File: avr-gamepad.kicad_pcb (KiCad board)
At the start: 2 copper layers, 29.7 x 55.6 mm, 31 parts, among them J1 Conn_01x08, P1 USB_C_Plug_USB2.0, SW10 Up, SW11 Down, SW12 Left, SW13 Select, SW2 R, SW3 X, SW4 A, SW5 B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

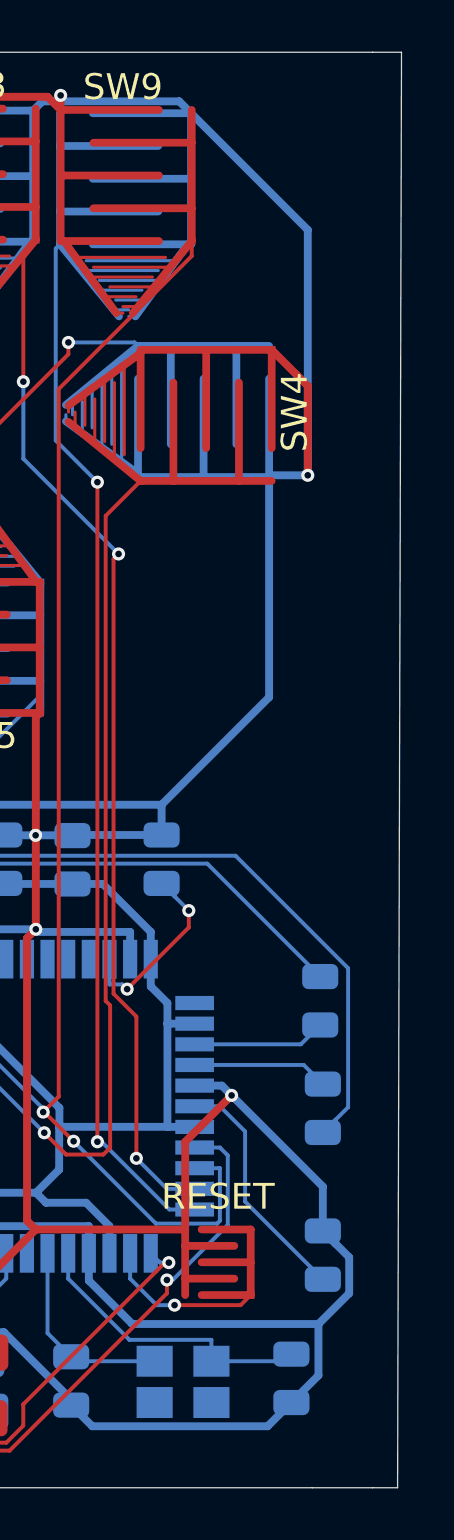
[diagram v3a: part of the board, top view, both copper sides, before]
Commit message: reduce outline
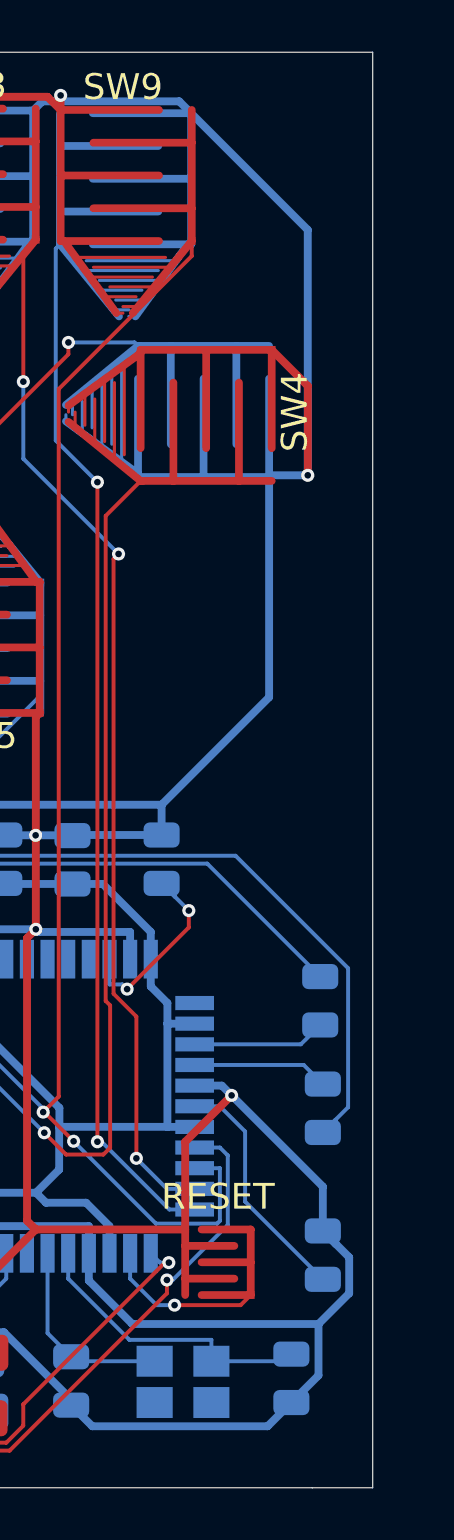
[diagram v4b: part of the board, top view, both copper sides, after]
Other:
- board size 29.7 x 55.6 mm -> 28.5 x 55.6 mm
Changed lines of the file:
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@@
   (general
     (thickness 0.1016)
-    (drawings 21)
+    (drawings 19)
     (tracks 490)
     (zones 0)
@@
       ))
   )
-  (gr_line (start 156.972 136.0424) (end 156.0068 136.0424) (layer Edge.Cuts) (width 0.05))
-  (gr_line (start 157.1244 80.4164) (end 156.972 136.0424) (layer Edge.Cuts) (width 0.05))
-  (gr_line (start 156.0068 80.4164) (end 157.1244 80.4164) (layer Edge.Cuts) (width 0.05))
+  (gr_line (start 156.0068 136.0424) (end 156.0068 80.4164) (layer Edge.Cuts) (width 0.05))
   (gr_line (start 127.4572 80.4164) (end 127.4826 102.0826) (layer Edge.Cuts) (width 0.05))
   (gr_line (start 127.4572 80.4164) (end 156.0068 80.4164) (layer Edge.Cuts) (width 0.05))

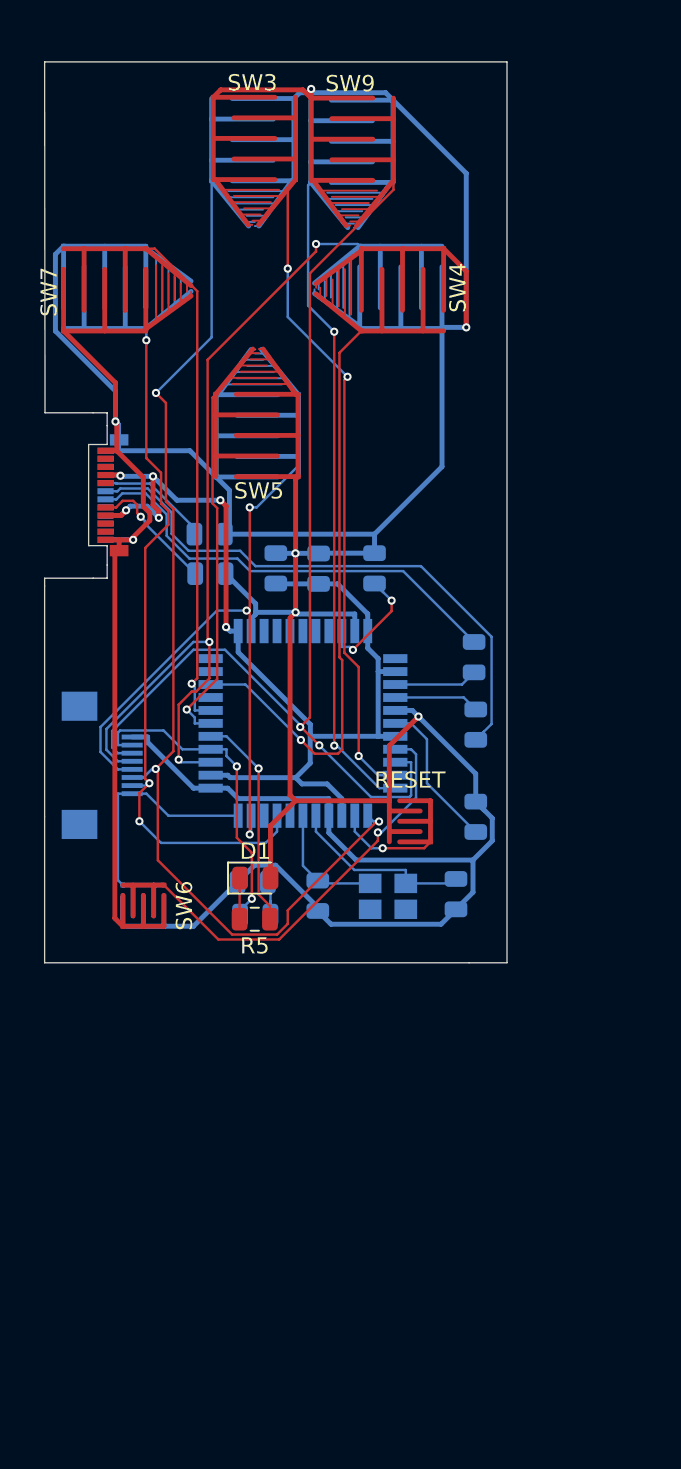
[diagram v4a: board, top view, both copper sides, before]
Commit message: pin swapping and component shuffling
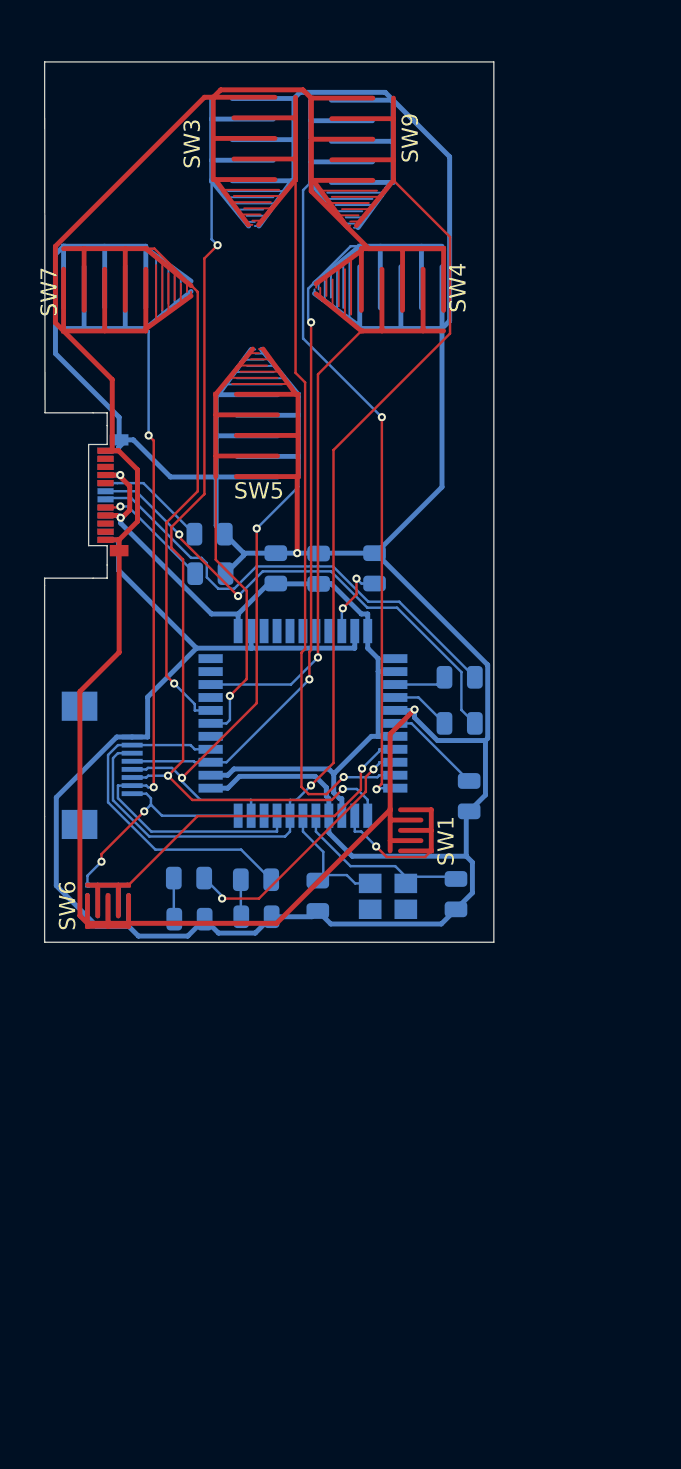
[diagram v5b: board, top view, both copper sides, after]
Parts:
- D1, R5: moved to B.Cu
- moved D1 4.79 mm to (136.4, 133.3)
- moved R5 4.79 mm to (136.4, 130.8)
- moved R6 2.18 mm to (140.5, 130.9), turned to 0 degrees
- moved SW13 2.18 mm to (131.4, 132.5)
- moved SW6 2.18 mm to (131.4, 132.5)
- moved D2 2.15 mm to (140.5, 133.2), turned to 0 degrees
- moved R4 1.53 mm to (153.1, 118.4), turned to 0 degrees
- moved C8 1.34 mm to (153.7, 125.8), turned to 270 degrees
- moved R2 1.00 mm to (153.1, 121.3), turned to 0 degrees
- moved SW1 0.56 mm to (150.1, 127.9)
- renumbered RESET to SW1
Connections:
- J1 pad 6: /pb1 -> /pd0
- R5 pad 2: /pd7 -> /pb1
- SW9 pad 1: /pb1 -> /pd0
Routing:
- net /pd0: track 0.00 -> 61.9 mm, vias 0 -> 1
- net GND: track 250.8 -> 312.4 mm, vias 7 -> 2
- net /pb1: track 66.0 -> 16.5 mm
- net +5V: track 67.1 -> 51.9 mm, vias 6 -> 2
- net /pd7: track 13.8 -> 0.00 mm, vias 1 -> 0
- net /pd4: track 52.1 -> 41.6 mm, vias 3 -> 2
- net /pb7: track 65.8 -> 55.5 mm
- net /pd3: track 46.0 -> 35.9 mm, vias 3 -> 2
- net /pc6: track 36.5 -> 28.6 mm
- net Net-(P1-PadA6): track 35.9 -> 31.5 mm, vias 0 -> 2
- net /pb0: track 25.0 -> 20.7 mm
- net /pb2: track 40.5 -> 44.3 mm, vias 3 -> 1
- net Net-(C8-Pad1): track 9.34 -> 6.03 mm
- net Net-(C7-Pad1): track 8.01 -> 4.86 mm
- net Net-(R4-Pad1): track 5.71 -> 3.22 mm
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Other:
- board size 28.5 x 55.6 mm -> 27.7 x 54.4 mm

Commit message: move footprints to new dir, increase contact size, add squidward
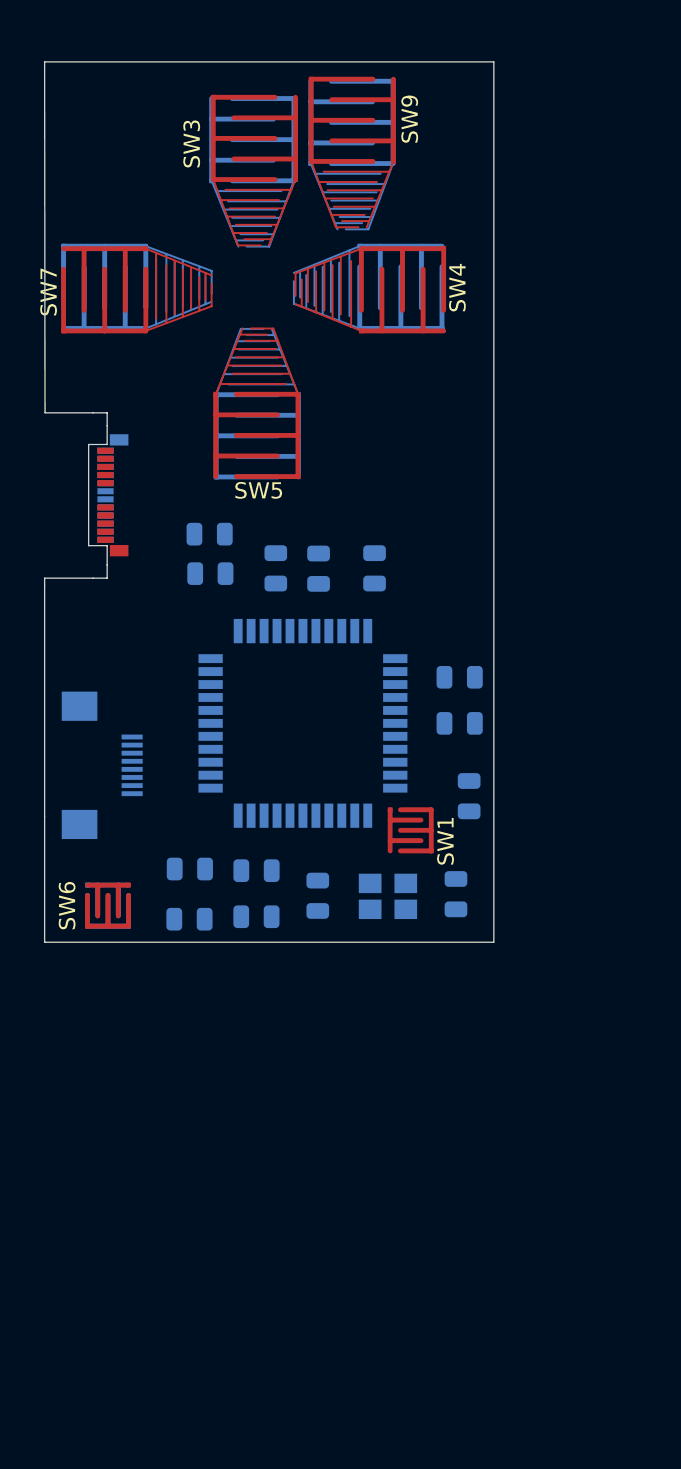
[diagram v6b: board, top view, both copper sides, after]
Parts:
- added ?: , squidward:loser_silkscreen, B.Cu at (143.3, 121.2)
- SW1, SW13, SW6: footprint Button Contacts:Small -> button-contacts:Small
- SW10, SW11, SW12, SW2, SW3, SW4, SW5, SW7, SW8, SW9: footprint Button Contacts:Large_tapered -> button-contacts:Large_tapered
- moved SW2 1.17 mm to (146.4, 84.2)
- moved SW9 1.17 mm to (146.5, 84.0)
- moved R5 0.56 mm to (136.4, 130.3)
- moved R6 0.56 mm to (140.5, 130.4)
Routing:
- net GND: track 312.4 -> 0.00 mm, vias 2 -> 0
- net /pd0: track 61.9 -> 0.00 mm, vias 1 -> 0
- net /pb7: track 55.5 -> 0.00 mm, vias 3 -> 0
- net +5V: track 51.9 -> 0.00 mm, vias 2 -> 0
- net /pb2: track 44.3 -> 0.00 mm, vias 1 -> 0
- net /pd1: track 43.2 -> 0.00 mm, vias 2 -> 0
- net /pd4: track 41.6 -> 0.00 mm, vias 2 -> 0
- net /pb3: track 41.0 -> 0.00 mm, vias 2 -> 0
- net /pd3: track 35.9 -> 0.00 mm, vias 2 -> 0
- net /pb5: track 32.7 -> 0.00 mm, vias 1 -> 0
- net Net-(P1-PadA6): track 31.5 -> 0.00 mm, vias 2 -> 0
- net Net-(P1-PadA7): track 29.1 -> 0.00 mm
- net /pc6: track 28.6 -> 0.00 mm, vias 1 -> 0
- net /pb4: track 22.6 -> 0.00 mm, vias 1 -> 0
- net /pd6: track 21.7 -> 0.00 mm
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
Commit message: kill the double sided feature, make it 2 boards, import mousebites
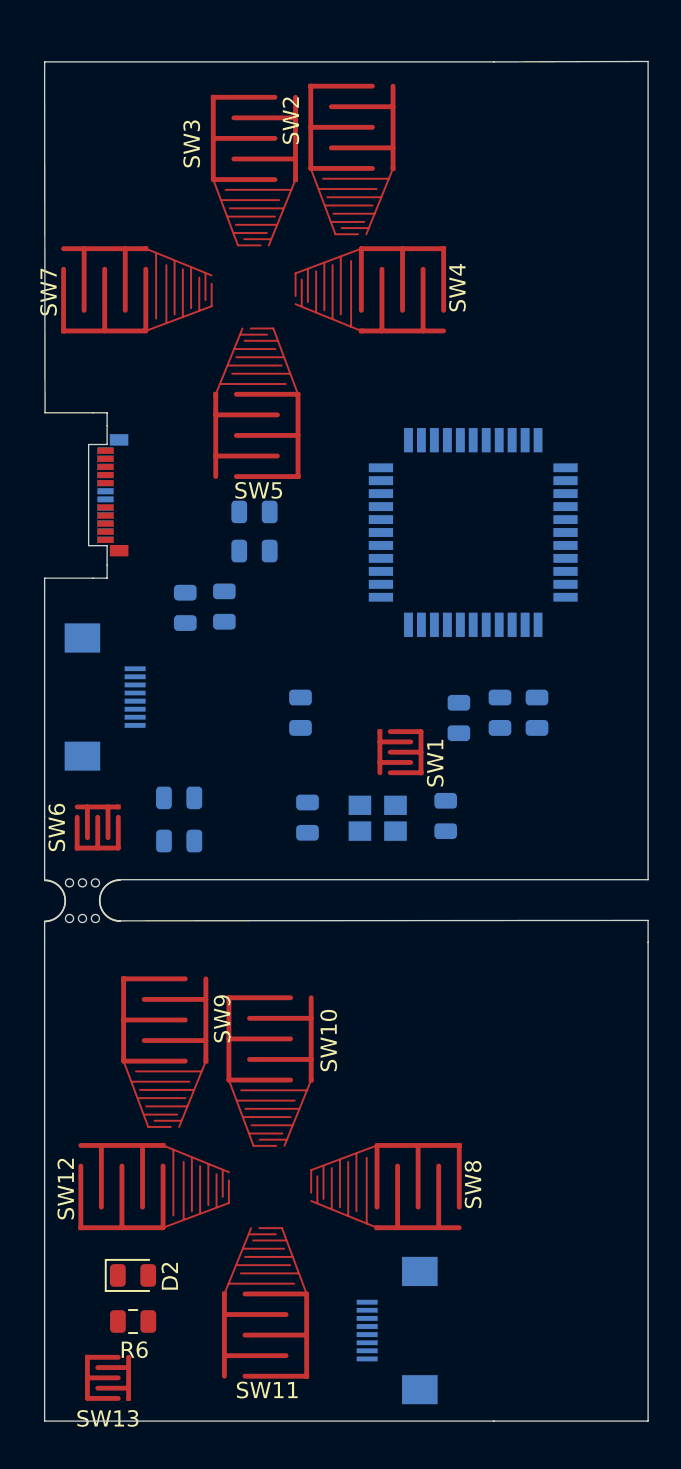
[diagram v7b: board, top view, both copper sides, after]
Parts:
- removed ?: , squidward:loser_silkscreen
- added J2: Conn_01x08, Connector_FFC-FPC:Hirose_FH12-8S-0.5SH_1x08-1MP_P0.50mm_Horizontal, B.Cu at (131.2, 119.6)
- added mouse-bite-2.54mm-slot: VAL**, Panelization:mouse-bite-2.54mm-slot, F.Cu at (129.8, 132.2)
- D2, R6, SW10, SW11, SW12, SW13, SW2, SW8: moved to F.Cu
- moved SW8 58.8 mm to (150.5, 149.9)
- moved SW12 58.1 mm to (132.2, 149.9)
- moved SW9 56.7 mm to (134.9, 139.6)
- moved SW10 55.5 mm to (141.4, 140.7), turned to 0 degrees
- moved SW11 55.5 mm to (141.1, 159.0), turned to 180 degrees
- moved J1 39.4 mm to (149.2, 158.8), turned to 270 degrees
- moved SW13 29.2 mm to (131.4, 161.7), turned to 0 degrees
- moved R6 28.9 mm to (132.9, 158.2)
- moved D2 23.4 mm to (132.9, 155.3)
- moved R2 18.2 mm to (140.4, 108.2), turned to 180 degrees
- moved C1 16.5 mm to (155.6, 120.6)
- moved C4 16.2 mm to (157.9, 120.6)
- moved U1 15.8 mm to (153.9, 109.5), turned to 0 degrees
- moved R4 14.9 mm to (140.4, 110.6), turned to 180 degrees
- moved C7 10.0 mm to (143.3, 120.6)
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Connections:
- D2 pad 2: GND -> Net-(D2-Pad2)
- J1 pad 1: /pd5 -> Net-(J1-Pad1)
- J1 pad 2: /pd1 -> Net-(J1-Pad2)
- J1 pad 3: /pb7 -> Net-(J1-Pad3)
- J1 pad 4: /pd3 -> Net-(J1-Pad4)
- J1 pad 5: /pd4 -> Net-(J1-Pad5)
- J1 pad 6: /pd0 -> Net-(J1-Pad6)
- J1 pad 7: /pd6 -> Net-(J1-Pad7)
- J1 pad 8: GND -> Net-(D2-Pad2)
- R6 pad 2: /pd6 -> Net-(J1-Pad7)
- SW10 pad 1: /pb7 -> Net-(J1-Pad3)
- SW10 pad 2: GND -> Net-(D2-Pad2)
- SW11 pad 1: /pd3 -> Net-(J1-Pad4)
- SW11 pad 2: GND -> Net-(D2-Pad2)
- SW12 pad 1: /pd4 -> Net-(J1-Pad5)
- SW12 pad 2: GND -> Net-(D2-Pad2)
- SW13 pad 1: /pd5 -> Net-(J1-Pad1)
- SW13 pad 2: GND -> Net-(D2-Pad2)
- SW8 pad 1: /pd1 -> Net-(J1-Pad2)
- SW8 pad 2: GND -> Net-(D2-Pad2)
- SW9 pad 1: /pd0 -> Net-(J1-Pad6)
- SW9 pad 2: GND -> Net-(D2-Pad2)
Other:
- board size 27.7 x 54.4 mm -> 37.3 x 83.9 mm

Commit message: component relabelling, shuffling around, two-piece board
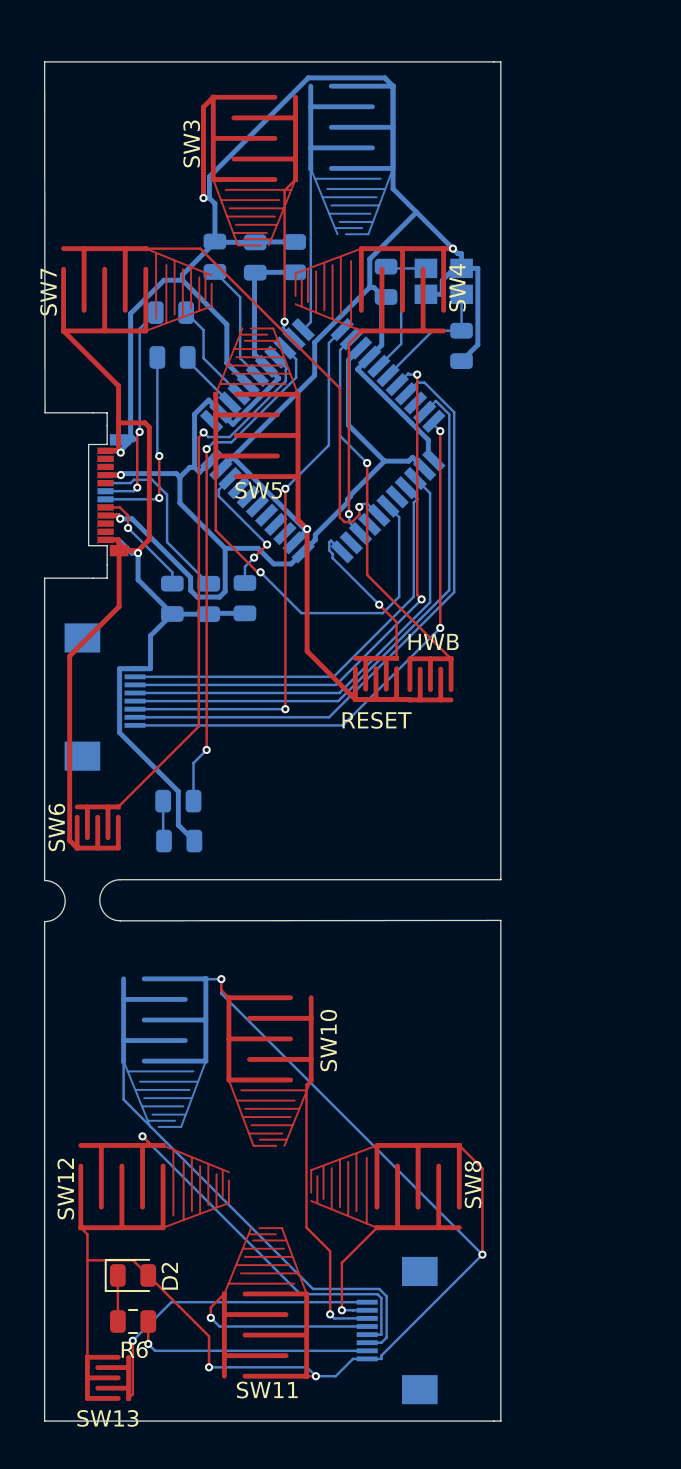
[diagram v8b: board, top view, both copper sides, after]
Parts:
- removed C7: 0.1uF, Capacitor_SMD:C_0805_2012Metric
- removed C8: 1uF, Capacitor_SMD:C_0805_2012Metric
- removed mouse-bite-2.54mm-slot: VAL**, Panelization:mouse-bite-2.54mm-slot
- added C2: 1uF, Capacitor_SMD:C_0805_2012Metric, B.Cu at (142.9, 92.5)
- added C3: 10pF, Capacitor_SMD:C_0805_2012Metric, B.Cu at (153.2, 98.0)
- added RESET: SW_Push, button-contacts:Small, F.Cu at (147.9, 118.5)
- C4: value 1uF -> 10pF
- C5: value 10pF -> 0.1uF
- C6: value 10pF -> 1uF
- R1: value 5.1k -> 22
- R4: value 22 -> 5.1k
- SW2, SW9: moved to B.Cu
- Y1: value 16 MHz -> Crystal_GND24
- moved C6 37.4 mm to (138.0, 92.4), turned to 90 degrees
- moved Y1 33.4 mm to (152.1, 94.0), turned to 180 degrees
- moved C1 31.9 mm to (140.5, 92.5)
- moved C4 28.2 mm to (148.5, 94.0), turned to 270 degrees
- moved R1 18.4 mm to (135.3, 95.9), turned to 180 degrees
- moved C5 14.1 mm to (139.8, 113.5)
- moved U1 10.9 mm to (144.6, 103.8), turned to 315 degrees
- moved R2 10.8 mm to (135.4, 98.7)
- moved HWB 4.86 mm to (151.3, 118.5), turned to 270 degrees
- moved R4 4.09 mm to (137.6, 113.6), turned to 270 degrees
- moved R3 0.98 mm to (135.3, 113.6)
- moved R5 0.21 mm to (135.7, 126.1)
- turned SW2 to 180 degrees
- turned SW9 to 180 degrees
- renumbered SW1 to HWB
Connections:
- C4 pad 1: +5V -> Net-(C4-Pad1)
- R1 pad 1: Net-(P1-PadB5) -> Net-(R1-Pad1)
- R1 pad 2: GND -> Net-(P1-PadA6)
- R2 pad 2: Net-(P1-PadA6) -> Net-(P1-PadA7)
- R3 pad 1: Net-(P1-PadA5) -> Net-(P1-PadB5)
- R4 pad 1: Net-(R4-Pad1) -> Net-(P1-PadA5)
- R4 pad 2: Net-(P1-PadA7) -> GND
- U1 pad 16: Net-(C6-Pad1) -> Net-(C4-Pad1)
- U1 pad 17: Net-(C5-Pad1) -> Net-(C3-Pad1)
- U1 pad 3: Net-(R4-Pad1) -> Net-(R2-Pad1)
- U1 pad 4: Net-(R2-Pad1) -> Net-(R1-Pad1)
- U1 pad 42: Net-(C7-Pad1) -> Net-(C5-Pad1)
- U1 pad 6: Net-(C8-Pad1) -> Net-(C6-Pad1)
- Y1 pad 1: Net-(C5-Pad1) -> Net-(C3-Pad1)
- Y1 pad 2: Net-(C6-Pad1) -> GND
- Y1 pad 3: (no net) -> Net-(C4-Pad1)
- Y1 pad 4: (no net) -> GND
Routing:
- net GND: track 0.00 -> 214.1 mm, vias 0 -> 5
- net Net-(D2-Pad2): track 0.00 -> 73.8 mm, vias 0 -> 4
- net +5V: track 0.00 -> 72.2 mm, vias 0 -> 2
- net /pd1: track 0.00 -> 38.0 mm
- net /pd0: track 0.00 -> 35.4 mm, vias 0 -> 2
- net /pd3: track 0.00 -> 35.2 mm
- net /pd5: track 0.00 -> 34.3 mm, vias 0 -> 2
- net /pb7: track 0.00 -> 34.2 mm, vias 0 -> 2
- net /pb0: track 0.00 -> 33.7 mm, vias 0 -> 1
- net /pb1: track 0.00 -> 31.5 mm, vias 0 -> 2
- net /pd4: track 0.00 -> 28.6 mm
- net /pb4: track 0.00 -> 28.2 mm, vias 0 -> 1
- net Net-(J1-Pad6): track 0.00 -> 27.5 mm
- net /pb5: track 0.00 -> 27.1 mm, vias 0 -> 1
- net /pd6: track 0.00 -> 26.4 mm
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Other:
- board size 37.3 x 83.9 mm -> 28.2 x 83.9 mm
